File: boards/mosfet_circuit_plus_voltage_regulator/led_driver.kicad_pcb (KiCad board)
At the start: 2 copper layers, 75 x 50 mm, 26 parts, among them J1 Vin, J2 LED, J3 control_in, Q1 N_chan_mosfet, Q2 P-Chan_mosfet, U1 MC34063AP

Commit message: little board clean up, adding license and date
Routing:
- net Net-(C1-Pad1): track 4.21 -> 3.71 mm
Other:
- board text added: "CERN OHL v1.2 by amchagas 20190729"
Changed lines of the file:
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@@
   (general
     (thickness 1.6)
-    (drawings 12)
-    (tracks 140)
+    (drawings 13)
+    (tracks 139)
     (zones 0)
     (modules 26)
@@
     (descr "TO-220-2, Vertical, RM 5.08mm, see https://www.centralsemi.com/PDFS/CASE/TO-220-2PD.PDF")
     (tags "TO-220-2 Vertical RM 5.08mm")
-    (fp_text reference R7 (at 2.54 -4.27 180) (layer F.SilkS)
+    (fp_text reference R7 (at 7 2.35 180) (layer F.SilkS)
       (effects (font (size 1 1) (thickness 0.15)))
     )
@@
       (rotate (xyz 0 0 0))
     )
+  )
+  (gr_text "CERN OHL v1.2\nby amchagas\n20190729" (at 126.25 57.75) (layer F.SilkS)
+    (effects (font (size 1.5 1.5) (thickness 0.3)))
   )
   (gr_text 1 (at 129.4 69.4 270) (layer F.SilkS)
@@
   (segment (start 139.92 96.08) (end 139.92 99.6) (width 1) (layer F.Cu) (net 4))
   (segment (start 139.84 96) (end 139.92 96.08) (width 1) (layer F.Cu) (net 4))
-  (segment (start 124.714 71.0052) (end 124.3584 71.3608) (width 0.75) (layer F.Cu) (net 5))
   (segment (start 124.714 67.2968) (end 124.714 71.0052) (width 0.75) (layer B.Cu) (net 5))
   (segment (start 120.500001 84.200001) (end 121.5 85.2) (width 0.75) (layer F.Cu) (net 6))

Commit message: load board with kicad6
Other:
- net class Default removed
- net class power_line removed
- net class thick removed

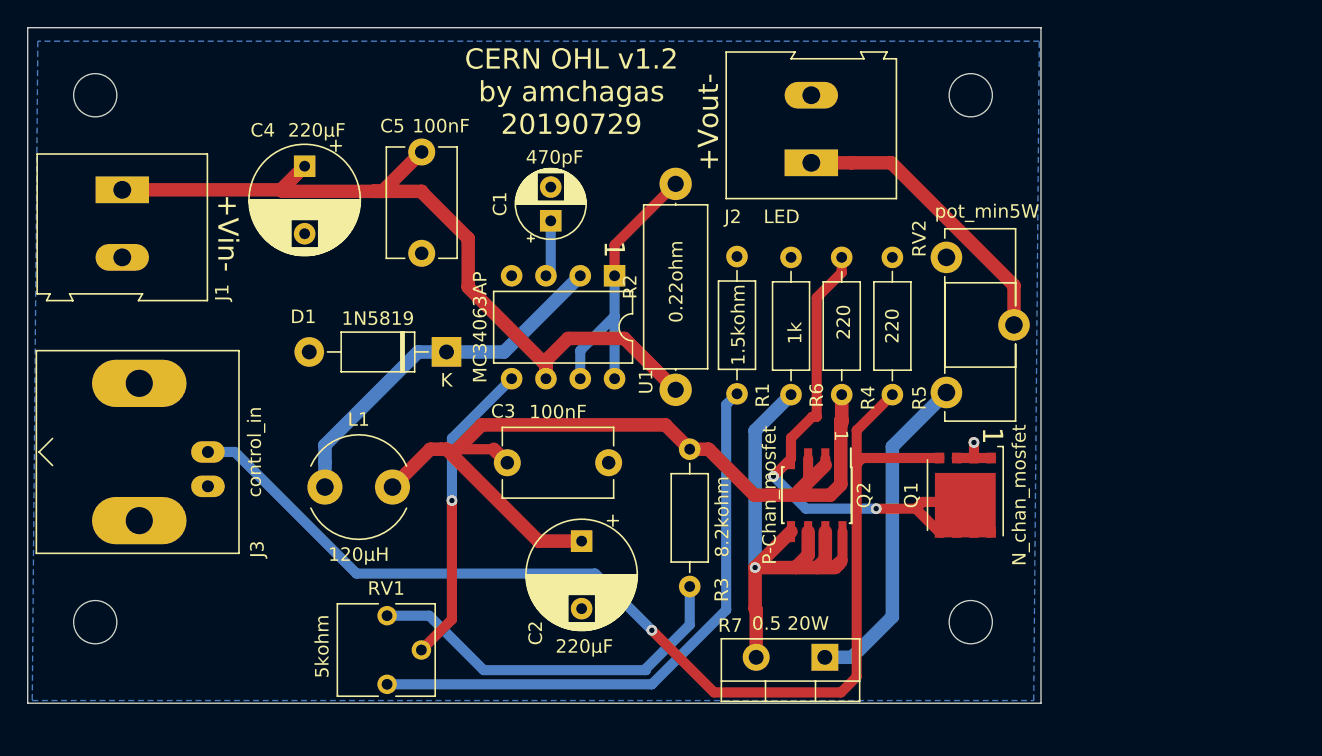
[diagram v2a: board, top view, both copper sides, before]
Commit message: update mosfets on led driver board
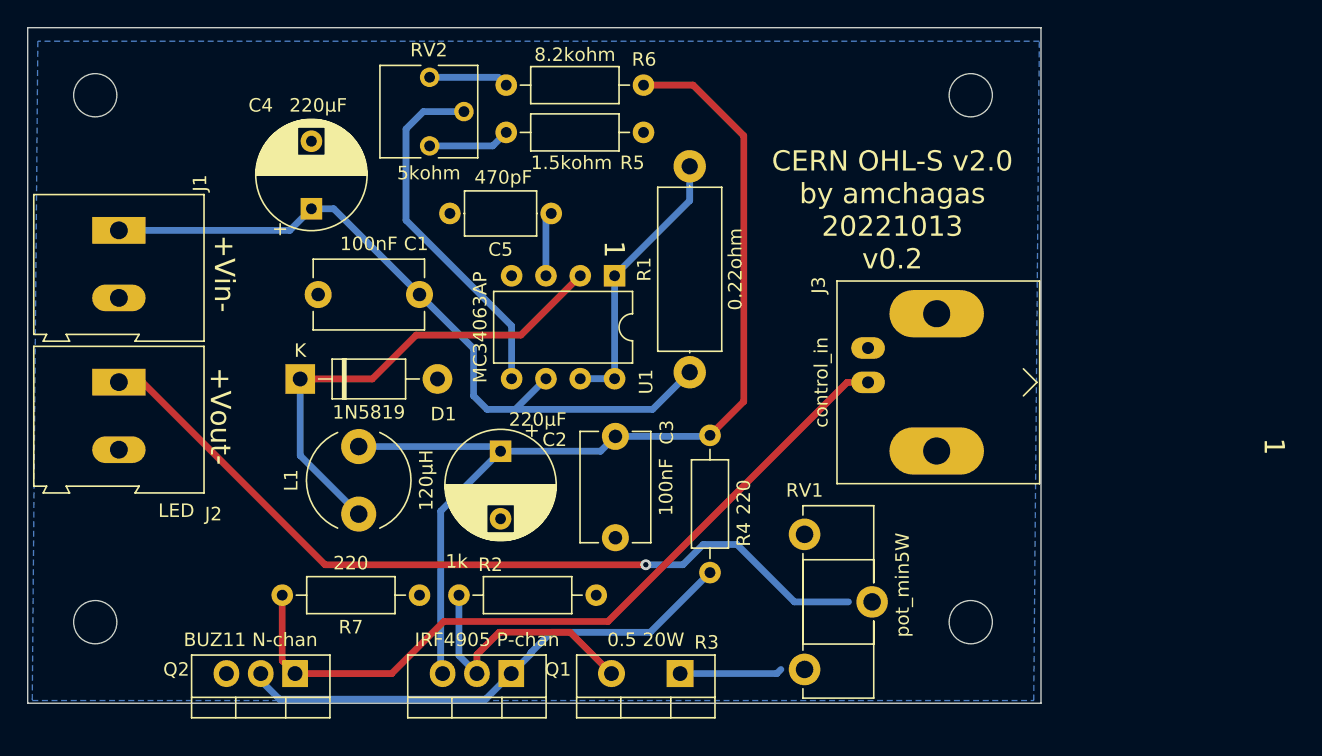
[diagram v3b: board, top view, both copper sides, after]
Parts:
- C1: value 470pF -> 100nF; footprint Capacitor_THT:CP_Radial_D5.0mm_P2.50mm -> Capacitor_THT:C_Disc_D8.0mm_W5.0mm_P7.50mm
- C5: value 100nF -> 470pF; footprint Capacitor_THT:C_Disc_D8.0mm_W5.0mm_P7.50mm -> Capacitor_THT:C_Axial_L5.1mm_D3.1mm_P7.50mm_Horizontal
- Q1: value N_chan_mosfet -> IRF4905 P-chan; footprint Package_TO_SOT_SMD:TDSON-8-1 -> Package_TO_SOT_THT:TO-220-3_Vertical
- Q2: value P-Chan_mosfet -> BUZ11 N-chan; footprint Package_SO:SOIC-8_3.9x4.9mm_P1.27mm -> Package_TO_SOT_THT:TO-220-3_Vertical
- R1: value 1.5kohm -> 0.22ohm; footprint Resistor_THT:R_Axial_DIN0207_L6.3mm_D2.5mm_P10.16mm_Horizontal -> Resistor_THT:R_Axial_DIN0414_L11.9mm_D4.5mm_P15.24mm_Horizontal
- R2: value 0.22ohm -> 1k; footprint Resistor_THT:R_Axial_DIN0414_L11.9mm_D4.5mm_P15.24mm_Horizontal -> Resistor_THT:R_Axial_DIN0207_L6.3mm_D2.5mm_P10.16mm_Horizontal
- R3: value 8.2kohm -> 0.5 20W; footprint Resistor_THT:R_Axial_DIN0207_L6.3mm_D2.5mm_P10.16mm_Horizontal -> Package_TO_SOT_THT:TO-220-2_Vertical
- R5: value 220 -> 1.5kohm
- R6: value 1k -> 8.2kohm
- R7: value 0.5 20W -> 220; footprint Package_TO_SOT_THT:TO-220-2_Vertical -> Resistor_THT:R_Axial_DIN0207_L6.3mm_D2.5mm_P10.16mm_Horizontal
- RV1: value 5kohm -> pot_min5W; footprint Potentiometer_THT:Potentiometer_Vishay_T73YP_Vertical -> Potentiometer_THT:Potentiometer_ACP_CA14-H5_Horizontal
- RV2: value pot_min5W -> 5kohm; footprint Potentiometer_THT:Potentiometer_ACP_CA14-H5_Horizontal -> Potentiometer_THT:Potentiometer_Vishay_T73YP_Vertical
- moved J2 53.8 mm to (92.8, 79.2), turned to -90 degrees
- moved J3 49.1 mm to (148.2, 79.2), turned to -90 degrees
- moved Q2 40.8 mm to (105.8, 100.8), turned to 180 degrees
- moved RV2 39.1 mm to (115.8, 61.8)
- moved Q1 36.1 mm to (121.8, 100.8), turned to 180 degrees
- moved RV1 32.8 mm to (143.5, 90.5)
- moved R7 30.4 mm to (115.0, 95.0)
- moved R5 30.0 mm to (121.4, 60.8), turned to 0 degrees
- moved R6 25.4 mm to (131.6, 57.2), turned to 180 degrees
- moved R4 25.3 mm to (136.5, 93.3), turned to 90 degrees
- moved R2 22.1 mm to (117.9, 95.0), turned to 0 degrees
- moved R3 16.6 mm to (134.3, 100.8), turned to 180 degrees
- moved C1 11.1 mm to (115.0, 72.8), turned to 180 degrees
- moved D1 11.0 mm to (106.2, 79.0), turned to 0 degrees
- moved C5 10.6 mm to (124.8, 66.8), turned to 180 degrees
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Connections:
- C1 pad 1: Net-(C1-Pad1) -> VDD
- C5 pad 1: VDD -> Net-(C5-Pad1)
- Q1 pad 1: GND -> Net-(Q1-Pad1)
- Q1 pad 2: GND -> Net-(Q1-Pad2)
- Q1 pad 3: GND -> Net-(C2-Pad1)
- Q2 pad 1: Net-(C2-Pad1) -> Net-(J3-Pad1)
- Q2 pad 2: Net-(C2-Pad1) -> Net-(Q1-Pad1)
- Q2 pad 3: Net-(C2-Pad1) -> GND
- R1 pad 1: Net-(R1-Pad1) -> VDD
- R1 pad 2: GND -> Net-(R1-Pad2)
- R2 pad 1: VDD -> Net-(Q1-Pad2)
- R2 pad 2: Net-(R2-Pad2) -> GND
- R3 pad 1: Net-(C2-Pad1) -> Net-(R3-Pad1)
- R3 pad 2: Net-(R3-Pad2) -> Net-(Q1-Pad2)
- R4 pad 1: Net-(Q1-Pad5) -> Net-(Q1-Pad1)
- R5 pad 1: GND -> Net-(R5-Pad1)
- R5 pad 2: Net-(J3-Pad1) -> GND
- R6 pad 1: Net-(Q2-Pad5) -> Net-(C2-Pad1)
- R6 pad 2: GND -> Net-(R6-Pad2)
- R7 pad 1: Net-(R7-Pad1) -> GND
- R7 pad 2: Net-(Q2-Pad5) -> Net-(J3-Pad1)
- RV1 pad 1: Net-(R1-Pad1) -> unconnected-(RV1-Pad1)
- RV1 pad 2: Net-(RV1-Pad2) -> Net-(J2-Pad1)
- RV1 pad 3: Net-(R3-Pad2) -> Net-(R3-Pad1)
- RV2 pad 1: (no net) -> Net-(R5-Pad1)
- RV2 pad 2: Net-(J2-Pad1) -> Net-(RV2-Pad2)
- RV2 pad 3: Net-(R7-Pad1) -> Net-(R6-Pad2)
- U1 pad 1: Net-(R2-Pad2) -> Net-(R1-Pad2)
- U1 pad 3: Net-(C1-Pad1) -> Net-(C5-Pad1)
- U1 pad 5: Net-(RV1-Pad2) -> Net-(RV2-Pad2)
- U1 pad 7: Net-(R2-Pad2) -> Net-(R1-Pad2)
- U1 pad 8: Net-(R2-Pad2) -> Net-(R1-Pad2)
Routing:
- net Net-(R1-Pad1): track 43.7 -> 0.00 mm
- net Net-(Q1-Pad5): track 40.9 -> 0.00 mm, vias 2 -> 0
- net Net-(J2-Pad1): track 21.7 -> 62.0 mm, vias 0 -> 1
- net Net-(Q2-Pad5): track 39.1 -> 0.00 mm, vias 1 -> 0
- net Net-(Q1-Pad1): track 0.00 -> 38.3 mm
- net Net-(R3-Pad2): track 28.4 -> 0.00 mm
- net Net-(J3-Pad1): track 84.4 -> 57.5 mm, vias 1 -> 0
- net Net-(RV2-Pad2): track 0.00 -> 26.5 mm
- net Net-(R7-Pad1): track 24.5 -> 0.00 mm
- net Net-(RV1-Pad2): track 22.8 -> 0.00 mm, vias 1 -> 0
- net Net-(R2-Pad2): track 22.0 -> 0.00 mm
- net Net-(R1-Pad2): track 0.00 -> 20.6 mm
- net Net-(Q1-Pad2): track 0.00 -> 19.7 mm
- net Net-(D1-Pad1): track 27.2 -> 35.7 mm
- net Net-(R3-Pad1): track 0.00 -> 7.59 mm
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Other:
- board text added: "CERN OHL-S v2.0 by amchagas 20221013 v0.2"
- board text removed: "CERN OHL v1.2 by amchagas 20190729"

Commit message: update gerbers
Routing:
- net Net-(R3-Pad1): track 7.59 -> 9.34 mm
- net Net-(J2-Pad1): track 62.0 -> 63.7 mm
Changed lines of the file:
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@@
   (segment (start 94.485 79.235) (end 108 92.75) (width 0.5) (layer "F.Cu") (net 2))
   (via (at 131.75 92.75) (size 0.8) (drill 0.4) (layers "F.Cu" "B.Cu") (net 2))
-  (segment (start 142.75 95.5) (end 146.75 95.5) (width 0.5) (layer "B.Cu") (net 2))
+  (segment (start 142.75 95.5) (end 148.5 95.5) (width 0.5) (layer "B.Cu") (net 2))
+  (segment (start 136 91.25) (end 138.5 91.25) (width 0.5) (layer "B.Cu") (net 2))
+  (segment (start 131.75 92.75) (end 134.5 92.75) (width 0.5) (layer "B.Cu") (net 2))
   (segment (start 138.5 91.25) (end 142.75 95.5) (width 0.5) (layer "B.Cu") (net 2))
-  (segment (start 131.75 92.75) (end 134.5 92.75) (width 0.5) (layer "B.Cu") (net 2))
   (segment (start 134.5 92.75) (end 136 91.25) (width 0.5) (layer "B.Cu") (net 2))
-  (segment (start 136 91.25) (end 138.5 91.25) (width 0.5) (layer "B.Cu") (net 2))
   (segment (start 139 61) (end 139 80.67) (width 0.5) (layer "F.Cu") (net 3))
   (segment (start 135.25 57.25) (end 139 61) (width 0.5) (layer "F.Cu") (net 3))
@@
   (segment (start 126.8984 78.9808) (end 129.4384 78.9808) (width 0.5) (layer "B.Cu") (net 10))
   (segment (start 129.4384 71.3608) (end 129.4384 78.9808) (width 0.5) (layer "B.Cu") (net 10))
+  (segment (start 141.75 100.5) (end 143.5 100.5) (width 0.5) (layer "B.Cu") (net 11))
   (segment (start 134.29 100.805) (end 141.445 100.805) (width 0.5) (layer "B.Cu") (net 11))
   (segment (start 141.445 100.805) (end 141.75 100.5) (width 0.5) (layer "B.Cu") (net 11))
